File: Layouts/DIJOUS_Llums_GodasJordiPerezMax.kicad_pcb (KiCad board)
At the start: 2 copper layers, 81 parts, among them J1 Conn_01x05_Socket, J10 Screw_Terminal_01x02, J11 Conn_01x06, J5 Conn_01x05, J6 Conn_01x03, J7 Conn_01x02, J8 DE9_Plug, J9 Conn_01x06_Socket, Q3 Si7336ADP, Q4 Si7336ADP, Q7 Si7336ADP, Q8 Si7336ADP, U2 LM2596T-ADJ, U3 PIC18F2580-I/SO, U4 MCP2551-I-SN, U7 PCA9306D

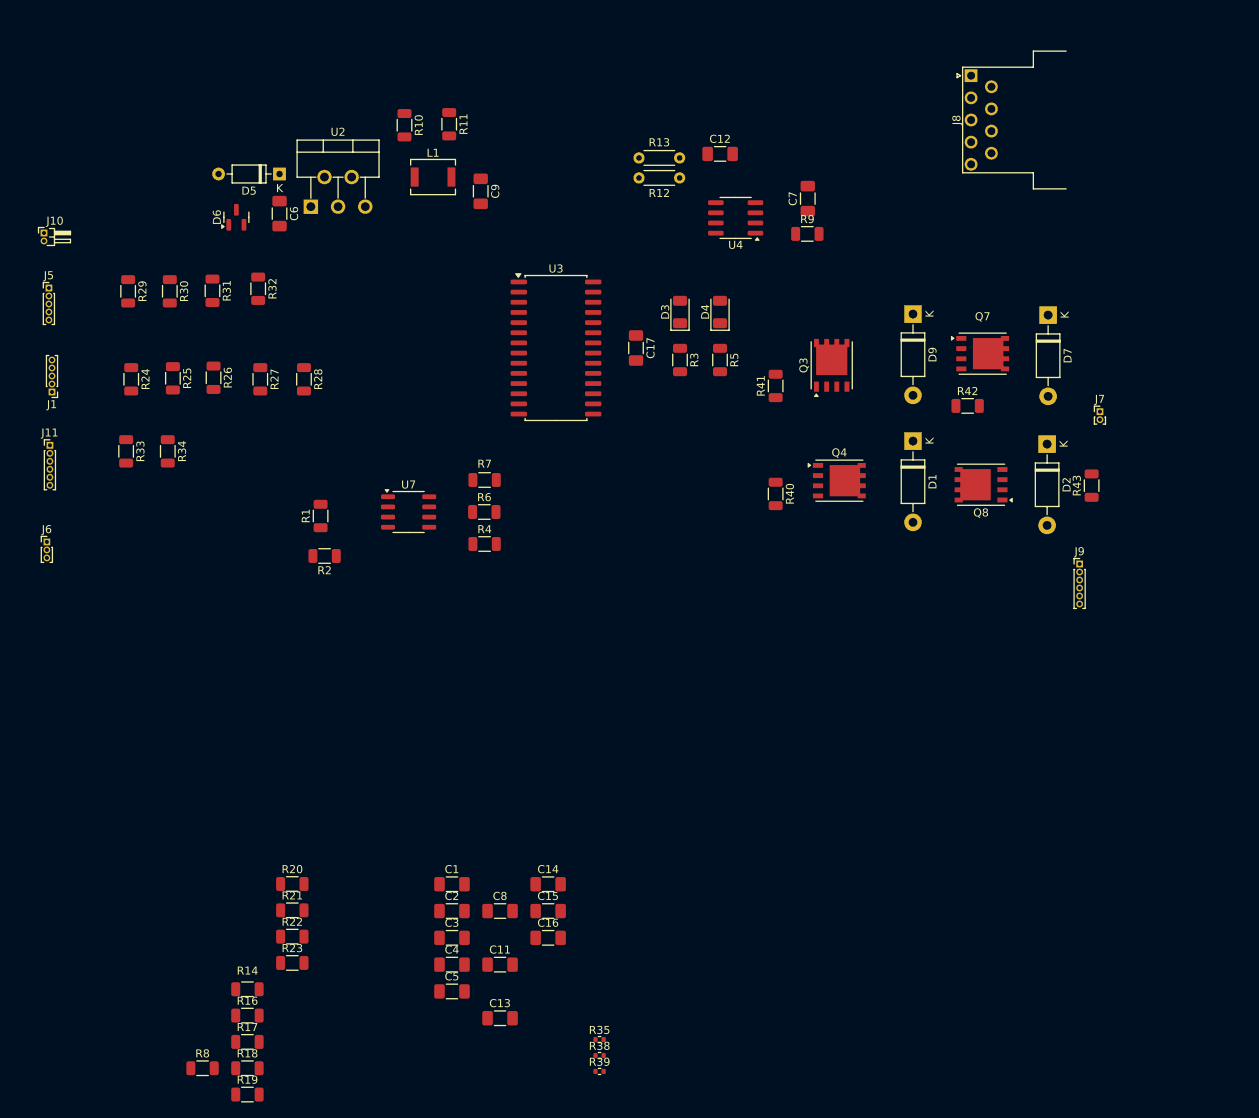
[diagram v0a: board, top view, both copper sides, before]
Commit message: Update DIJOUS_Llums_GodasJordiPerezMax.kicad_pcb
Primer avance en PCB. Se ha hecho Placement de una parte de los componentes, separación de planos de masa y potencia y el routing del Buck, del puente H, algunas conexiones del micro e inputs y outputs.
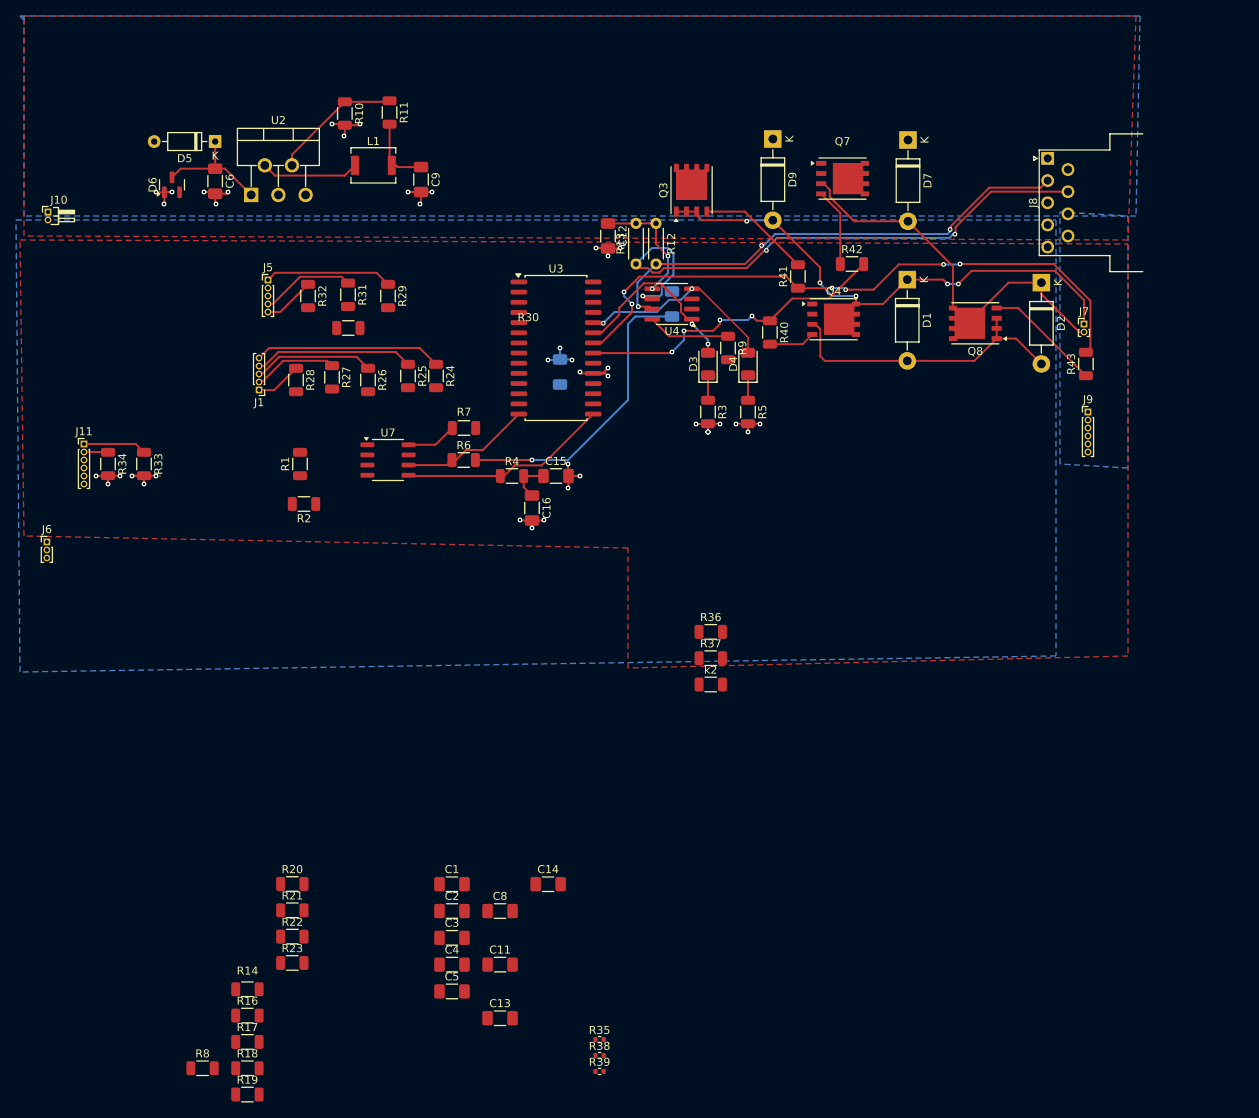
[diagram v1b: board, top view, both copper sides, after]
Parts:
- added R36: 1k, Resistor_SMD:R_1206_3216Metric, F.Cu at (97.8, 89.0)
- added R37: 100, Resistor_SMD:R_1206_3216Metric, F.Cu at (97.8, 92.3)
- added k2: 1k, Resistor_SMD:R_1206_3216Metric, F.Cu at (97.8, 95.6)
- C17, C7: moved to B.Cu
- moved C15 54.4 mm to (78.5, 69.5)
- moved C16 53.8 mm to (75.5, 73.5), turned to -90 degrees
- moved R24 38.1 mm to (63.5, 57.0)
- moved R29 32.5 mm to (57.5, 47.0)
- moved R25 29.4 mm to (60.0, 57.0)
- moved D9 28.0 mm to (105.6, 27.4)
- moved Q3 28.0 mm to (95.4, 33.8)
- moved Q7 28.0 mm to (114.3, 32.3)
- moved D7 28.0 mm to (122.5, 27.5)
- moved J5 27.4 mm to (42.5, 45.0)
- moved J1 25.9 mm to (41.4, 58.8)
- moved R42 22.9 mm to (115.5, 43.0)
- moved R30 22.8 mm to (52.5, 51.0), turned to 0 degrees
- moved C7 21.5 mm to (93.0, 48.0)
- moved D1 20.2 mm to (122.4, 45.0)
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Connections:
- net CANRX renamed CAN+
- net CANTX renamed CAN-
- net SCL_O renamed SCL_O+
- net SDA_O renamed SDA_O-
- J6 pad 1: RA5 -> RB5
- J8 pad 2: CANL_O -> CANO+
- J8 pad 5: unconnected-(J8-Pad5) -> GND
- J8 pad 7: CANH_O -> CANO-
- R12 pad 2: CANH_O -> CANO+
- R13 pad 1: CANL_O -> CANO-
- R14 pad 2: RA5 -> RB5
- U3 pad 26: unconnected-(U3-RB5/KBI1/PGM-Pad26) -> RB5
- U4 pad 6: CANL_O -> CANO-
- U4 pad 7: CANH_O -> CANO+
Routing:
- net Motor_in1: track 0.00 -> 79.1 mm, vias 0 -> 6
- net CANO-: track 0.00 -> 74.5 mm, vias 0 -> 3
- net Motor_o1: track 0.00 -> 64.8 mm, vias 0 -> 5
- net CANO+: track 0.00 -> 63.0 mm, vias 0 -> 3
- net Motor_o2: track 0.00 -> 51.6 mm
- net VDD-trans: track 0.00 -> 42.9 mm, vias 0 -> 1
- net Motor_in2: track 0.00 -> 39.9 mm, vias 0 -> 4
- net Shunt_in: track 0.00 -> 37.5 mm
- net GND: track 0.00 -> 34.6 mm, vias 0 -> 26
- net SDA_O-: track 0.00 -> 26.3 mm
- net CAN+: track 0.00 -> 25.6 mm, vias 0 -> 2
- net RC0: track 0.00 -> 23.5 mm
- net CAN-: track 0.00 -> 22.9 mm, vias 0 -> 2
- net RC1: track 0.00 -> 20.0 mm
- net GNDPWR: track 0.00 -> 17.6 mm, vias 0 -> 12
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- added copper zone on F.Cu, net +12V
- added copper zone on F.Cu, net +Vcc
- added copper zone on B.Cu, net GND
- added copper zone on B.Cu, net GNDPWR

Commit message: Update DIJOUS_Llums_GodasJordiPerezMax.kicad_pcb
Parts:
- removed the C1 at (65.5, 120.5)
- removed C12: 47nF, Capacitor_SMD:C_1206_3216Metric_Pad1.33x1.80mm_HandSolder
- removed the C5 at (65.5, 133.9)
- removed the D1 at (122.4, 45.0)
- removed the D2 at (139.2, 45.3)
- removed D9: 1N5817, Diode_THT:D_DO-41_SOD81_P10.16mm_Horizontal
- removed J11: Conn_01x06, Connector_PinHeader_1.00mm:PinHeader_1x06_P1.00mm_Vertical
- removed the J8 at (140.0, 29.8)
- removed the R12 at (91.0, 37.9)
- removed R24, R25: 1k, Resistor_SMD:R_1206_3216Metric
- removed the R26 at (55.0, 57.5)
- removed the R27 at (50.5, 57.2)
- removed the R28 at (46.0, 57.5)
- removed the R29 at (57.5, 47.0)
- removed the R30 at (52.5, 51.0)
- removed the R31 at (52.5, 46.8)
- removed the R32 at (47.5, 47.0)
- removed the R33 at (27.0, 68.0)
- removed the R40 at (105.2, 51.6)
- removed the R41 at (108.7, 44.6)
- removed the R42 at (115.5, 43.0)
- added ?: , , F.Cu at (150.5, 30.6)
- added ?: , , F.Cu at (57.1, 99.2)
- added ?: , , F.Cu at (150.2, 99.3)
- added C16: 100nF, Capacitor_SMD:C_1206_3216Metric_Pad1.33x1.80mm_HandSolder, F.Cu at (122.8, 39.6)
- added C17: 100nF, Capacitor_SMD:C_1206_3216Metric_Pad1.33x1.80mm_HandSolder, F.Cu at (100.2, 85.0)
- added C4: 100nF, Capacitor_SMD:C_1206_3216Metric_Pad1.33x1.80mm_HandSolder, F.Cu at (88.5, 98.7)
- added CR1: SS3P5HM3/84A, SS3P5:CR_5HM3&slash_84A_VIS, F.Cu at (145.9, 61.8)
- added D5: 1N5817, Diode_THT:D_DO-41_SOD81_P10.16mm_Horizontal, F.Cu at (106.3, 33.8)
- added D6: 1N5817, Diode_THT:D_DO-41_SOD81_P10.16mm_Horizontal, F.Cu at (103.8, 45.7)
- added D8: 1N5817, Diode_THT:D_DO-41_SOD81_P10.16mm_Horizontal, F.Cu at (138.7, 48.0)
- added J2: Conn_01x03, Connector_PinHeader_1.00mm:PinHeader_1x03_P1.00mm_Vertical, F.Cu at (102.0, 29.2)
- added J3: Conn_01x06, Connector_PinHeader_1.00mm:PinHeader_1x06_P1.00mm_Vertical, F.Cu at (94.6, 98.2)
- added K1: G5LE-1 DC12, G5LE-1-DC12:RELAY_G5LE-1 DC5_OMR, F.Cu at (63.7, 36.8)
- added K2: G5LE-1 DC12, G5LE-1-DC12:RELAY_G5LE-1 DC5_OMR, F.Cu at (63.6, 60.2)
- added Q1: ZXTN19020DFFTA, ZXTN:ZXTN19020DFFTA_DIO, F.Cu at (74.9, 38.2)
- added Q2: ZXTN19020DFFTA, ZXTN:ZXTN19020DFFTA_DIO, F.Cu at (74.7, 42.9)
- added Q5: Si7336ADP, Package_SO:PowerPAK_SO-8_Single, F.Cu at (116.0, 39.2)
- added Q6: ZXTN19020DFFTA, ZXTN:ZXTN19020DFFTA_DIO, F.Cu at (74.7, 48.0)
- added Q9: Si7336ADP, Package_SO:PowerPAK_SO-8_Single, F.Cu at (132.7, 39.2)
- added R1: 1k, Resistor_SMD:R_1206_3216Metric, F.Cu at (76.1, 79.5)
- added R16: 1k, Resistor_SMD:R_1206_3216Metric, F.Cu at (98.1, 36.6)
- added R19: 1k, Resistor_SMD:R_1206_3216Metric, F.Cu at (119.3, 80.5)
- added R2: 1k, Resistor_SMD:R_1206_3216Metric, F.Cu at (75.8, 82.9)
- added R22: 47k, Resistor_SMD:R_1206_3216Metric, F.Cu at (121.5, 70.1)
- added R35: 1k, Resistor_SMD:R_1206_3216Metric, F.Cu at (121.9, 63.2)
- added R37: 10k, Resistor_SMD:R_0402_1005Metric, F.Cu at (110.9, 58.5)
- added R38: 10k, Resistor_SMD:R_0402_1005Metric, F.Cu at (119.0, 62.7)
- added R4: 1k, Resistor_SMD:R_1206_3216Metric, F.Cu at (92.9, 92.4)
- added R44: 10k, Resistor_SMD:R_0402_1005Metric, F.Cu at (116.2, 61.2)
- added R45: 1k, Resistor_SMD:R_1206_3216Metric, F.Cu at (125.3, 63.2)
- added R46: 1k, Resistor_SMD:R_1206_3216Metric, F.Cu at (113.5, 61.8)
- added R47: 100, Resistor_SMD:R_1206_3216Metric, F.Cu at (78.5, 59.3)
- added R6: 1k, Resistor_SMD:R_1206_3216Metric, F.Cu at (98.9, 88.8)
- added R8: 220, Resistor_SMD:R_1206_3216Metric, F.Cu at (102.7, 41.4)
- added REF**: MountingHole_3.2mm_M3_DIN965_Pad, MountingHole:MountingHole_3.2mm_M3_DIN965_Pad, F.Cu at (57.0, 30.5)
- added U5: MCP2551-I-SN, Package_SO:SOIC-8_3.9x4.9mm_P1.27mm, F.Cu at (119.1, 75.2)
- added U6: ADM7172ACPZ-5.0-R7, ADM7172ACPZ-5.0-R7:CP-8-21_ADI, F.Cu at (149.0, 73.4)
- added U7: LT6202CS5, LT6202CS5:S_5_ADI, F.Cu at (125.0, 44.6)
- added XTAL1: XT9M20ANA8M, XT9M20HRR8M:XTAL_ANA8M_VIS, F.Cu at (78.9, 69.6)
- C7: moved to F.Cu
- J4: renamed from J10; footprint Connector_PinHeader_1.00mm:PinHeader_1x02_P1.00mm_Horizontal -> Connector_PinHeader_1.00mm:PinHeader_1x02_P1.00mm_Vertical
- J6: value Conn_01x03 -> DE9_Plug; footprint Connector_PinHeader_1.00mm:PinHeader_1x03_P1.00mm_Vertical -> Connector_Dsub:DSUB-9_Female_Horizontal_P2.77x2.54mm_EdgePinOffset9.40mm
- Q3, Q7: value Si7336ADP -> ZXTN19020DFFTA; footprint Package_SO:PowerPAK_SO-8_Single -> ZXTN:ZXTN19020DFFTA_DIO
- R13: value 60 -> 1k; footprint Resistor_THT:R_Axial_DIN0204_L3.6mm_D1.6mm_P5.08mm_Horizontal -> Resistor_SMD:R_1206_3216Metric
- R14: value 220 -> 100
- R17, R18: value 100 -> 1k
- R43: value 1k -> 10k; footprint Resistor_SMD:R_1206_3216Metric -> Resistor_SMD:R_0402_1005Metric
- R9: value 47k -> 1k
- U4: value MCP2551-I-SN -> ADP7112ACBZ-3.3-R7; footprint Package_SO:SOIC-8_3.9x4.9mm_P1.27mm -> ADP7112ACBZ-3.3-R7:CB-6-15_ADI-M
- moved J4 133.4 mm to (148.4, 36.6), turned to 90 degrees
- moved J6 127.7 mm to (142.4, 83.0)
- moved D1 117.3 mm to (151.4, 48.3), turned to 90 degrees
- moved D2 116.7 mm to (146.8, 42.6), turned to 0 degrees
- moved R17 114.3 mm to (94.2, 39.6), turned to 180 degrees
- moved C6 112.1 mm to (147.1, 47.1), turned to 180 degrees
- moved R26 107.6 mm to (81.3, 37.6), turned to 90 degrees
- moved R41 106.8 mm to (81.3, 48.4), turned to 90 degrees
- moved R18 106.7 mm to (115.4, 68.1), turned to 180 degrees
- moved R20 106.6 mm to (151.5, 62.8), turned to 180 degrees
- moved U3 106.3 mm to (145.3, 51.6), turned to -90 degrees
- moved R40 106.3 mm to (121.3, 44.5), turned to -90 degrees
- moved R39 104.3 mm to (129.2, 47.9), turned to 180 degrees
- moved R21 103.9 mm to (151.6, 68.4), turned to 180 degrees
- moved R32 101.4 mm to (126.0, 47.8), turned to 90 degrees
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- renumbered C3 to C1, C8 to C10, C13 to C11, C14 to C13, C17 to C14, C16 to C15, C15 to C2, C2 to C3, C4 to C5, C9 to C8, C11 to C9, D5 to D1, D6 to D2, J9 to J8, R2 to R10, R7 to R11, R4 to R12, R6 to R15, R10 to R20, R11 to R21, R16 to R26, R21 to R27, R8 to R28, R23 to R29, R22 to R30, R20 to R31, R35 to R32, R36 to R33, k2 to R36, R38 to R39, R39 to R40, R19 to R41, R37 to R42, R1 to R7, U7 to U1, U3 to U2, U2 to U3
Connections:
- net Net-(Q8-G) renamed /BJTbase12
- net SCL renamed SCl
- net SCL_O+ renamed SCL_O
- net SDA_O- renamed SDA_O
- C1 pad 2: VREF1 -> +3.3V
- C10 pad 1: VDD-trans -> +5V
- C11 pad 1: Net-(U5-SS) -> Net-(U4-SS)
- C14 pad 1: +Vcc -> +5V
- C15 pad 1: VDD-trans -> +5V
- C2 pad 1: VDD-trans -> +5V
- C7 pad 1: VDD-trans -> +5V
- C9 pad 1: VREF1 -> +3.3V
- D3 pad 1: Net-(D3-K) -> /LEDTX
- D3 pad 2: CAN- -> CANTX
- D4 pad 1: Net-(D4-K) -> /LEDRX
- D4 pad 2: CAN+ -> CANRX
- D7 pad 1: +12V -> Motor_o2
- D7 pad 2: Motor_o2 -> Shutin
- J4 pad 2: /fuse_node -> +12V
- J5 pad 2: +Vcc -> +5V
- J6 pad 1: RB5 -> unconnected-(J6-Pad1)
- J6 pad 2: GND -> CANL_O
- J6 pad 3: GND -> unconnected-(J6-Pad3)
- Q3 pad 1: Motor_o1 -> Net-(Q3-Pad1)
- Q3 pad 2: Motor_o1 -> Brushless
- Q3 pad 3: Motor_o1 -> +12V
- Q4 pad 1: Shunt_in -> Motor_o1
- Q4 pad 2: Shunt_in -> Motor_o1
- Q4 pad 3: Shunt_in -> Motor_o1
- Q4 pad 4: Net-(Q4-G) -> /BJTbase11
- Q4 pad 5: Motor_o1 -> +12V
- Q7 pad 1: Motor_o2 -> Net-(Q7-Pad1)
- Q7 pad 2: Motor_o2 -> Net-(K2-Pad2)
- Q7 pad 3: Motor_o2 -> +12V
- Q8 pad 1: Shunt_in -> Motor_o2
- Q8 pad 2: Shunt_in -> Motor_o2
- Q8 pad 3: Shunt_in -> Motor_o2
- Q8 pad 5: Motor_o2 -> +12V
- R10 pad 2: VREF1 -> +3.3V
- R11 pad 1: +12V -> +5V
- R12 pad 2: VDD-trans -> +5V
- R13 pad 1: CANO- -> MCLR
- R13 pad 2: Vref -> GND
- R14 pad 1: VDD-trans -> RA4
- R14 pad 2: RB5 -> Net-(Q6-Pad1)
- R15 pad 2: VDD-trans -> +5V
- R17 pad 1: RB5 -> PGC
- R17 pad 2: Net-(Q2-Pad1) (its old number) -> GND
- R18 pad 1: RB5 -> /LEDTX
- R18 pad 2: GNDPWR -> GND
- R26 pad 2: GNDPWR -> GND
- R27 pad 2: GNDPWR -> GND
- R28 pad 2: GNDPWR -> GND
- R3 pad 1: Net-(D3-K) -> RC2
- R31 pad 2: Net-(Q9-Pad1) -> Net-(Q3-Pad1)
- R32 pad 2: GNDPWR -> GND
- R34 pad 1: SDA -> Motor_in1
- R34 pad 2: GND -> /BJTbase11
- R36 pad 1: GNDPWR -> GND
- R39 pad 1: GNDPWR -> GND
- R41 pad 2: GNDPWR -> GND
- R42 pad 2: GNDPWR -> GND
- R43 pad 2: Motor_in1 -> GND
- R5 pad 1: Net-(D4-K) -> RC6
- R7 pad 2: VREF1 -> +3.3V
- R9 pad 1: Net-(U4-Rs) -> RC7
- U1 pad 2: VREF1 -> +3.3V
- U1 pad 7: VREF1 -> +5V
- U2 pad 20: +Vcc -> +5V
- U2 pad 23: CAN- -> CANTX
- U2 pad 24: CAN+ -> CANRX
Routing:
- net CANO-: track 74.5 -> 0.00 mm, vias 3 -> 0
- net CANO+: track 63.0 -> 0.00 mm, vias 3 -> 0
- net Motor_in1: track 79.1 -> 16.3 mm, vias 6 -> 0
- net Shutin: track 0.00 -> 59.1 mm, vias 0 -> 2
- net +12V: track 0.00 -> 50.5 mm, vias 0 -> 2
- net Low Beam: track 0.00 -> 46.7 mm
- net VDD-trans: track 42.9 -> 0.00 mm, vias 1 -> 0
- net Shunt_in: track 37.5 -> 0.00 mm
- net Motor_o1: track 64.8 -> 28.5 mm, vias 5 -> 0
- net RC7: track 5.74 -> 40.9 mm
- net GND: track 34.6 -> 0.00 mm, vias 26 -> 0
- net RB5: track 0.00 -> 33.7 mm
- net /BJTbase22: track 0.00 -> 32.1 mm
- net RA1: track 0.00 -> 31.5 mm
- net /BJTbase21: track 0.00 -> 29.9 mm, vias 0 -> 2
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- added copper zone on F.Cu, net +3.3V
- added copper zone on F.Cu, net +5V
- removed copper zone on F.Cu, net +Vcc
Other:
- board outline added: 102.1 x 77.1 mm

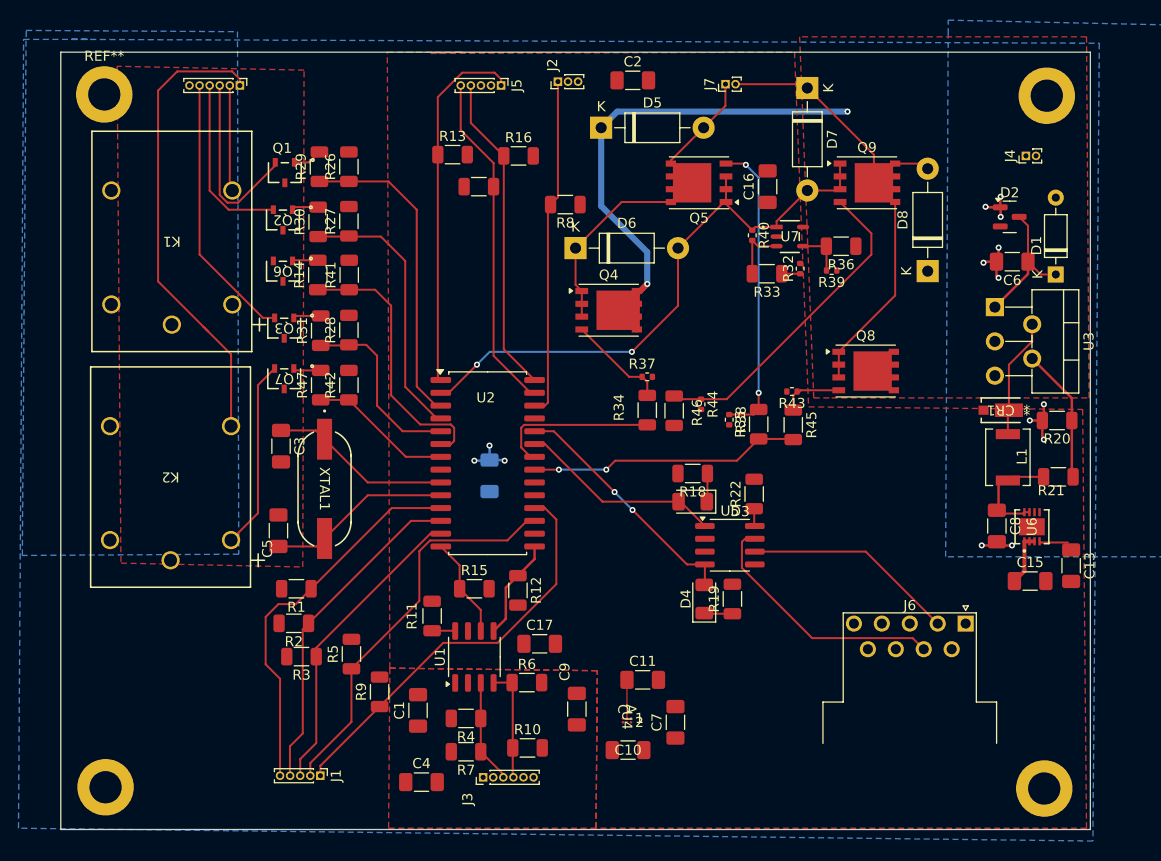
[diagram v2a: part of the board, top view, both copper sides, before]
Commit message: Update Layout
Versión 1.0 del Layout. En este Commit, se han ruteado algunos GND de SMD y mejorado la interconexión en algunos puntos concretos. A falta del okey del otro compañero
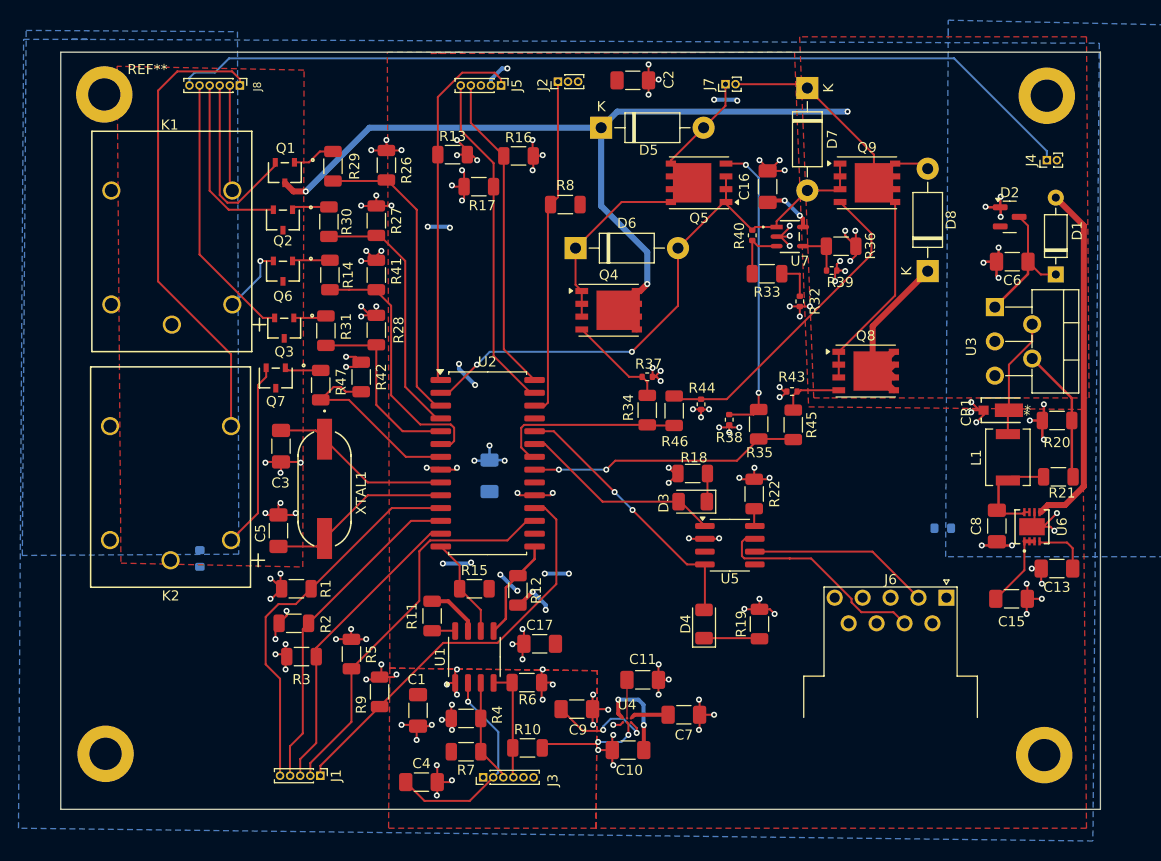
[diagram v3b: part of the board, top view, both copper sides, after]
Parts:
- added R23: 0, Resistor_SMD:R_0603_1608Metric, B.Cu at (66.5, 76.5)
- added R48: 0, Resistor_SMD:R_0603_1608Metric, B.Cu at (140.2, 73.5)
- moved R26 3.72 mm to (85.0, 37.5)
- moved R19 3.66 mm to (122.0, 83.0)
- moved ? 3.31 mm to (57.1, 95.9)
- moved ? 3.31 mm to (150.2, 96.0)
- moved R32 3.25 mm to (126.0, 51.0), turned to -90 degrees
- moved J6 3.20 mm to (140.5, 80.4)
- moved R27 2.72 mm to (84.0, 43.0)
- moved R28 2.72 mm to (84.0, 53.8)
- moved R41 2.69 mm to (84.0, 48.4)
- moved C15 2.55 mm to (147.0, 80.5)
- moved D4 2.48 mm to (116.5, 83.0)
- moved J4 2.12 mm to (150.5, 37.0)
- moved R42 1.46 mm to (82.5, 58.5)
- moved C13 1.44 mm to (151.5, 77.5), turned to 180 degrees
- moved R29 1.34 mm to (79.7, 37.6)
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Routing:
- net GND: track 0.00 -> 168.1 mm, vias 0 -> 122
- net GNDPWR: track 15.9 -> 118.5 mm, vias 11 -> 16
- net +12V: track 50.5 -> 141.0 mm, vias 2 -> 3
- net +5V: track 9.64 -> 57.4 mm, vias 3 -> 22
- net +3.3V: track 0.00 -> 42.8 mm, vias 0 -> 5
- net Net-(K1-Pad2): track 0.00 -> 6.75 mm, vias 0 -> 1
- net RA5: track 14.3 -> 19.0 mm
- net CANH_O: track 25.4 -> 21.9 mm
- net CANL_O: track 21.5 -> 18.5 mm
- net Net-(U6-SS): track 2.86 -> 5.59 mm
- net /LEDRX: track 2.82 -> 5.53 mm
- net Motor_in1: track 16.3 -> 19.0 mm
- net CANRX: track 24.4 -> 27.0 mm
- net Net-(R32-Pad1): track 1.83 -> 4.02 mm
- net RA2: track 27.0 -> 25.5 mm
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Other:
- board size 102.1 x 77.1 mm -> 103.1 x 75.1 mm
- board text added: "Do not mount!"
- board text added: "R17"

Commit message: Update Layout
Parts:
- removed ? (x3): , 
- added REF**: MountingHole_3.2mm_M3_DIN965_Pad, MountingHole:MountingHole_3.2mm_M3_DIN965_Pad, F.Cu at (150.5, 30.6)
- added REF**: MountingHole_3.2mm_M3_DIN965_Pad, MountingHole:MountingHole_3.2mm_M3_DIN965_Pad, F.Cu at (150.6, 97.0)
- added REF**: MountingHole_3.2mm_M3_DIN965_Pad, MountingHole:MountingHole_3.2mm_M3_DIN965_Pad, F.Cu at (57.1, 95.9)
- moved C4 0.87 mm to (87.9, 98.0)
- moved R7 0.42 mm to (92.9, 95.2)
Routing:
- net SCl: track 10.3 -> 11.2 mm
- net +3.3V: track 42.8 -> 42.2 mm
